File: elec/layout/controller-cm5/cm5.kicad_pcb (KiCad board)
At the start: 4 copper layers, 14 parts

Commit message: update layout, rename layout files with CM5 prefix
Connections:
- CN1 pad 12: cm5-line-7 -> cm5-line-3
- CN1 pad 15: line-1 -> line-2
- CN1 pad 17: line-2 -> line-6
- CN1 pad 19: cm5-line-4 -> cm5-line-2
- CN1 pad 20: line-6 -> line-1
- CN1 pad 23: cm5-line-5 -> cm5-line-1
- CN1 pad 25: cm5-line-2 -> cm5-line-4
- CN1 pad 27: line-7 -> line-3
- CN1 pad 40: line-3 -> line-7
- CN1 pad 41: line-4 -> line-5
- CN1 pad 78: cm5-line-3 -> cm5-line-7
- CN1 pad 80: cm5-line-1 -> cm5-line-5
- CN1 pad 81: line -> line-4
- CN1 pad 82: line-5 -> line
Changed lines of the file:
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@@
 	(net 0 "")
 	(net 1 "pins[20]")
-	(net 2 "cm5-line-3")
+	(net 2 "cm5-line-7")
 	(net 3 "cm5-pins[62]")
 	(net 4 "cm5.hdi_a-pins[74]")
@@
 	(net 7 "cm5.hdi_b-pins[74]")
 	(net 8 "cm5.hdi_a-pins[62]")
-	(net 9 "line-7")
+	(net 9 "line-3")
 	(net 10 "pins[18]")
 	(net 11 "cm5-pins[46]")
@@
 	(net 22 "cm5.hdi_a-pins[68]")
 	(net 23 "cm5.hdi_a-pins[92]")
-	(net 24 "line-4")
+	(net 24 "line-5")
 	(net 25 "pins[8]")
 	(net 26 "pins[1]")
@@
 	(net 28 "pins[90]")
 	(net 29 "pins[82]")
-	(net 30 "line-1")
+	(net 30 "line-2")
 	(net 31 "pins[58]")
 	(net 32 "SDA")
@@
 	(net 36 "cm5.hdi_a-pins[88]")
 	(net 37 "HDMI1_D2_P")
-	(net 38 "line-5")
+	(net 38 "line")
 	(net 39 "HDMI1_CK_N")
-	(net 40 "line-3")
+	(net 40 "line-7")
 	(net 41 "pins[86]")
 	(net 42 "cm5-pins[99]")
@@
 	(net 49 "cm5.hdi_b-pins[88]")
 	(net 50 "cm5.hdi_b-pins[92]")
-	(net 51 "cm5-line-4")
-	(net 52 "cm5-line-7")
+	(net 51 "cm5-line-2")
+	(net 52 "cm5-line-3")
 	(net 53 "pins[29]")
 	(net 54 "pins[49]")
@@
 	(net 71 "rj45.connector-net-1")
 	(net 72 "N_C_")
-	(net 73 "cm5-line-5")
+	(net 73 "cm5-line-1")
 	(net 74 "pins[3]")
 	(net 75 "HDMI0_CK_P")
@@
 	(net 80 "pins[41]")
 	(net 81 "pins[70]")
-	(net 82 "cm5-line-2")
+	(net 82 "cm5-line-4")
 	(net 83 "cm5.hdi_a-pins[98]")
 	(net 84 "cm5.hdi_b-pins[34]")
@@
 	(net 90 "pins[40]")
 	(net 91 "pins[91]")
-	(net 92 "line-6")
+	(net 92 "line-1")
 	(net 93 "pins[64]")
 	(net 94 "pins[9]")
@@
 	(net 116 "HDMI0_D2_P")
 	(net 117 "pins[22]")
-	(net 118 "line-2")
+	(net 118 "line-6")
 	(net 119 "pins[80]")
 	(net 120 "cm5.hdi_b-pins[94]")
@@
 	(net 125 "cm5.hdi_a-pins[94]")
 	(net 126 "cm5.hdi_a-pins[34]")
-	(net 127 "cm5-line-1")
+	(net 127 "cm5-line-5")
 	(net 128 "pins[61]")
 	(net 129 "cm5-pins[56]")
@@
 	(net 133 "pins[32]")
 	(net 134 "cm5.hdi_b-pins[93]")
-	(net 135 "line")
+	(net 135 "line-4")
 	(net 136 "cm5-pins[98]")
 	(net 137 "ETH_P0_P")
@@
 			(size 0.2 0.7)
 			(layers "F.Cu" "F.Paste" "F.Mask")
-			(net 52 "cm5-line-7")
+			(net 52 "cm5-line-3")
 		)
 		(pad "13" smd rect
@@
 			(size 0.2 0.7)
 			(layers "F.Cu" "F.Paste" "F.Mask")
-			(net 30 "line-1")
+			(net 30 "line-2")
 		)
 		(pad "16" smd rect
@@
 			(size 0.2 0.7)
 			(layers "F.Cu" "F.Paste" "F.Mask")
-			(net 118 "line-2")
+			(net 118 "line-6")
 		)
 		(pad "18" smd rect
@@
 			(size 0.2 0.7)
 			(layers "F.Cu" "F.Paste" "F.Mask")
-			(net 51 "cm5-line-4")
+			(net 51 "cm5-line-2")
 		)
 		(pad "20" smd rect
@@
 			(size 0.2 0.7)
 			(layers "F.Cu" "F.Paste" "F.Mask")
-			(net 92 "line-6")
+			(net 92 "line-1")
 		)
 		(pad "21" smd rect
@@
 			(size 0.2 0.7)
 			(layers "F.Cu" "F.Paste" "F.Mask")
-			(net 73 "cm5-line-5")
+			(net 73 "cm5-line-1")
 		)
 		(pad "24" smd rect
@@
 			(size 0.2 0.7)
 			(layers "F.Cu" "F.Paste" "F.Mask")
-			(net 82 "cm5-line-2")
+			(net 82 "cm5-line-4")
 		)
 		(pad "26" smd rect
@@
 			(size 0.2 0.7)
 			(layers "F.Cu" "F.Paste" "F.Mask")
-			(net 9 "line-7")
+			(net 9 "line-3")
 		)
 		(pad "28" smd rect
@@
 			(size 0.2 0.7)
 			(layers "F.Cu" "F.Paste" "F.Mask")
-			(net 40 "line-3")
+			(net 40 "line-7")
 		)
 		(pad "41" smd rect
@@
 			(size 0.2 0.7)
 			(layers "F.Cu" "F.Paste" "F.Mask")
-			(net 24 "line-4")
+			(net 24 "line-5")
 		)
 		(pad "42" smd rect
@@
 			(size 0.2 0.7)
 			(layers "F.Cu" "F.Paste" "F.Mask")
-			(net 2 "cm5-line-3")
+			(net 2 "cm5-line-7")
 		)
 		(pad "79" smd rect
@@
 			(size 0.2 0.7)
 			(layers "F.Cu" "F.Paste" "F.Mask")
-			(net 127 "cm5-line-1")
+			(net 127 "cm5-line-5")
 		)
 		(pad "81" smd rect
@@
 			(size 0.2 0.7)
 			(layers "F.Cu" "F.Paste" "F.Mask")
-			(net 135 "line")
+			(net 135 "line-4")
 		)
 		(pad "82" smd rect
@@
 			(size 0.2 0.7)
 			(layers "F.Cu" "F.Paste" "F.Mask")
-			(net 38 "line-5")
+			(net 38 "line")
 		)
 		(pad "83" smd rect

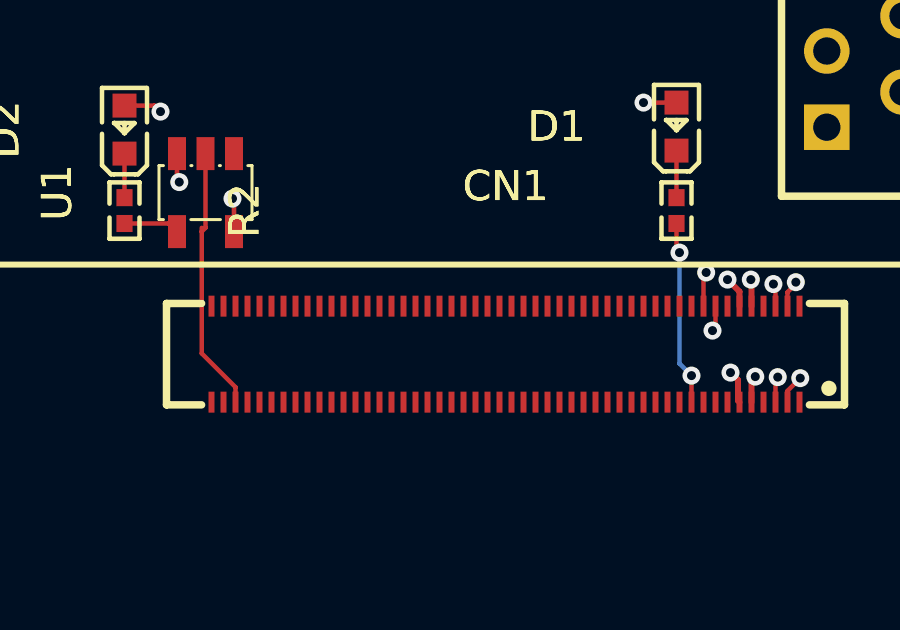
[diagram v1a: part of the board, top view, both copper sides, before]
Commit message: update layouts to kicad 9
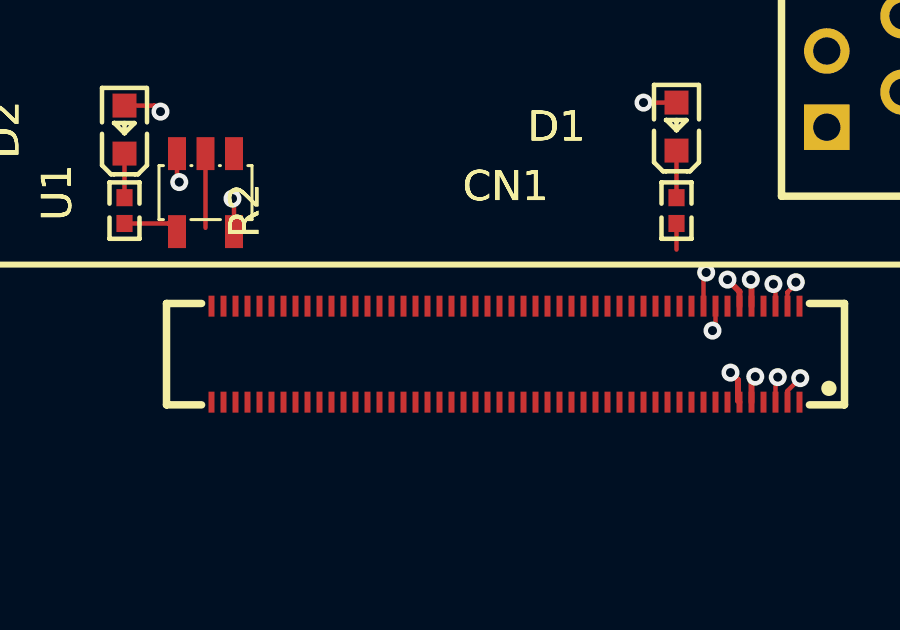
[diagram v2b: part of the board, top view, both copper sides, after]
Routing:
- net PWR_LED: track 8.93 -> 2.47 mm
- net pins[19]: track 6.16 -> 0.87 mm, vias 2 -> 0

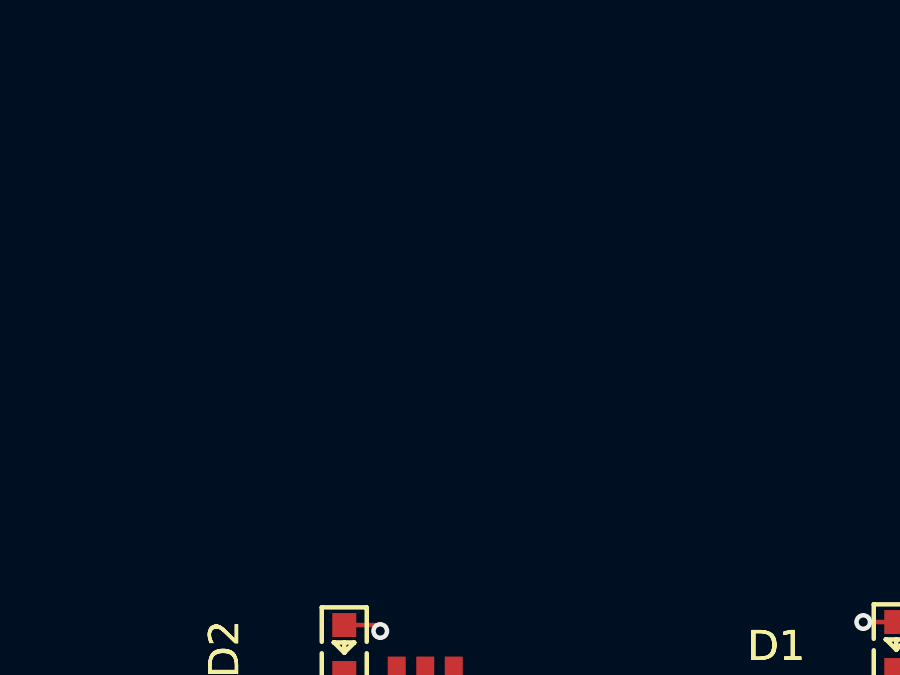
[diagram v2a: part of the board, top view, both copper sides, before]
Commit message: add power button and boot button, fix CAN layout
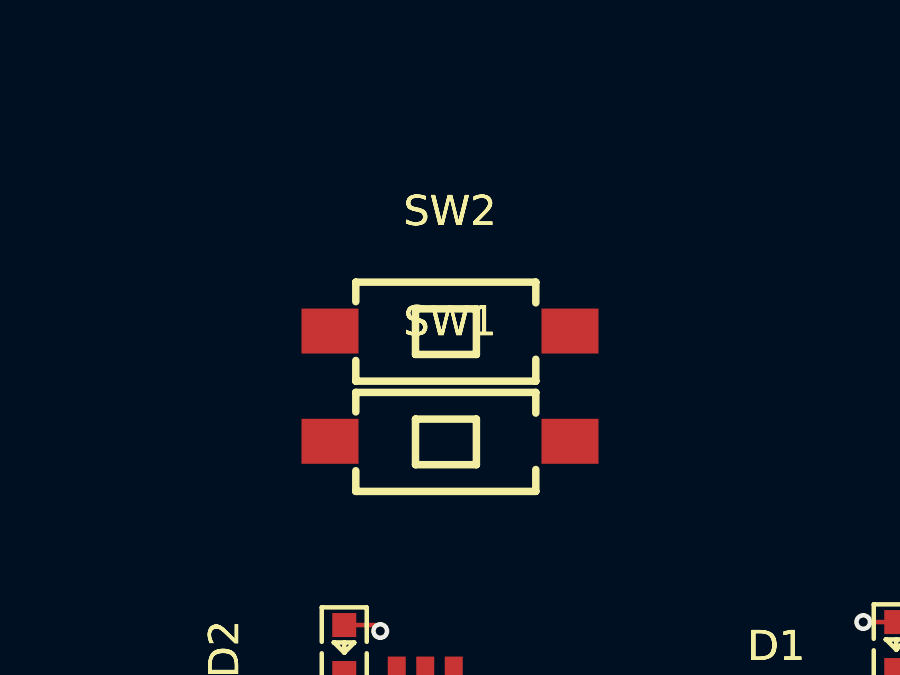
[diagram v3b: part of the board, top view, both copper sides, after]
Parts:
- added SW1: , atopile:SW-SMD_L6.0-W3.3-LS8.0-cfbaed, F.Cu at (140.7, 88.9)
- added SW2: , atopile:SW-SMD_L6.0-W3.3-LS8.0-cfbaed, F.Cu at (140.7, 85.2)
- R1, R2: value 10kΩ ±1% 62.5mW -> 2kΩ ±1% 62.5mW
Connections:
- net ETH_LED_ACTIVITY renamed line-31
- net ETH_LED_LINK renamed line-20
- net ETH_P0_N renamed line-41
- net ETH_P1_N renamed line-10
- net ETH_P1_P renamed line-28
- net ETH_P2_N renamed line-14
- net ETH_P3_N renamed line-37
- net ETH_P3_P renamed line-8
- net HDMI0_CK_N renamed pins[89]
- net HDMI0_CK_P renamed cm5-pins[87]
- net HDMI0_D0_N renamed pins[83]
- net HDMI0_D0_P renamed cm5-pins[81]
- net HDMI0_D1_N renamed pins[77]
- net HDMI0_D1_P renamed cm5-pins[75]
- net HDMI0_D2_N renamed cm5-pins[71]
- net HDMI0_D2_P renamed cm5-pins[69]
- net HDMI0_HOTPLUG renamed pins[52]
- net HDMI1_CEC renamed pins[48]
- net HDMI1_CK_N renamed pins[65]
- net HDMI1_CK_P renamed cm5-pins[63]
- net HDMI1_D0_N renamed pins[59]
- net HDMI1_D0_P renamed pins[57]
- net HDMI1_D1_N renamed pins[53]
- net HDMI1_D1_P renamed pins[51]
- net HDMI1_D2_P renamed pins[45]
- net HDMI1_HOTPLUG renamed pins[42]
- net SCL renamed line-9
- net SDA renamed line-34
- net UART_RX renamed line-26
- net UART_TX renamed line-12
- net USB2_D_N renamed line-38
- net VCC_1V8 renamed cm5-pins[87]-1
- net VCC_3V3 renamed hv
- net VCC_5V renamed pins[78]
- net cm5-line-6 renamed line-11
- net cm5-line-7 renamed cm5-pins[44]
- net cm5-pins[26] renamed line-30
- net cm5-pins[46] renamed pins[46]
- net cm5-pins[46]-1 renamed line-36
- net cm5-pins[68] renamed line-23
- net cm5.hdi_a-pins[34] renamed line-25
- net cm5.hdi_a-pins[56] renamed pins[56]
- net cm5.hdi_a-pins[62] renamed pins[62]
- net cm5.hdi_a-pins[68] renamed pins[68]
- net cm5.hdi_b-pins[26] renamed pins[26]
- net cm5.hdi_b-pins[34] renamed pins[34]
- net cm5.hdi_b-pins[92] renamed pins[92]
- net pins[20] renamed cm5.hdi_b-pins[20]
- net pins[23] renamed cm5.hdi_b-pins[23]
- net pins[29] renamed line-24
- net pins[39] renamed line-39
- net pins[41] renamed line-29
- net pins[43] renamed line-42
- net pins[44] renamed cm5-pins[44]-1
- net pins[58] renamed line-27
- net pins[63] renamed cm5.hdi_a-pins[63]
- net pins[64] renamed line-43
- net pins[69] renamed cm5.hdi_a-pins[69]
- net pins[70] renamed line-15
- net pins[71] renamed cm5.hdi_a-pins[71]
- net pins[75] renamed cm5.hdi_a-pins[75]
- net pins[95] renamed cm5.hdi_b-pins[95]
- CN1 pad 12: cm5-line-3 -> cm5-pins[23]
- CN1 pad 13: I2S_WS -> cm5-line-5
- CN1 pad 15: line-2 -> line-16
- CN1 pad 17: line-6 -> pins[33]
- CN1 pad 18: cm5.hdi_a-pins[35] -> line-7
- CN1 pad 19: cm5-line-2 -> line-17
- CN1 pad 20: line-1 -> line-21
- CN1 pad 23: cm5-line-1 -> line-6
- CN1 pad 24: pins[47] -> cm5-line-3
- CN1 pad 25: cm5-line-4 -> line-32
- CN1 pad 27: line-3 -> cm5-line-2
- CN1 pad 40: line-7 -> pins[79]
- CN1 pad 41: line-5 -> cm5.hdi_a-pins[81]
- CN1 pad 46: pins[91] -> line-33
- CN1 pad 48: PWR_LED -> cm5.hdi_a-pins[95]
- CN1 pad 53: cm5.hdi_a-pins[94] -> cm5-pins[94]
- CN1 pad 54: cm5.hdi_a-pins[92] -> line-13
- CN1 pad 6: ETH_P0_P -> line-4
- CN1 pad 75: pins[50] -> line-35
- CN1 pad 76: I2S_SCK -> cm5-line
- CN1 pad 80: cm5-line-5 -> cm5-line-1
- CN1 pad 81: line-4 -> line-22
- CN1 pad 82: line -> line-19
- CN1 pad 85: cm5-line -> line-18
- CN1 pad 88: I2S_SD -> cm5-line-4
- CN1 pad 90: gnd -> cm5-pins[20]
- CN1 pad 95: ETH_P2_P -> line
- CN2 pad 17: pins[33] -> line-40
- CN2 pad 18: cm5-pins[35] -> line-2
- CN2 pad 24: HDMI1_D2_N -> pins[47]
- CN2 pad 69: cm5-pins[62] -> line-1
- CN2 pad 72: cm5-pins[56] -> line-3
- CN2 pad 75: HDMI0_CEC -> pins[50]
- CN2 pad 98: USB2_D_P -> line-5
- R1 pad 2: pins[19] -> cm5-pins[20]
- RJ1 pad P2: ETH_P0_P -> line-4
- RJ1 pad P5: ETH_P2_P -> line
- U1 pad 2: PWR_LED -> cm5-pins[94]
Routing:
- net line-4: track 0.00 -> 16.5 mm, vias 0 -> 1
- net ETH_P0_P: track 16.5 -> 0.00 mm, vias 1 -> 0
- net line: track 0.00 -> 13.3 mm, vias 0 -> 1
- net ETH_P2_P: track 13.3 -> 0.00 mm, vias 1 -> 0
- net cm5-pins[94]: track 0.00 -> 2.47 mm
- net PWR_LED: track 2.47 -> 0.00 mm
- net pins[19]: track 0.87 -> 0.00 mm
- net cm5-pins[20]: track 0.00 -> 0.87 mm

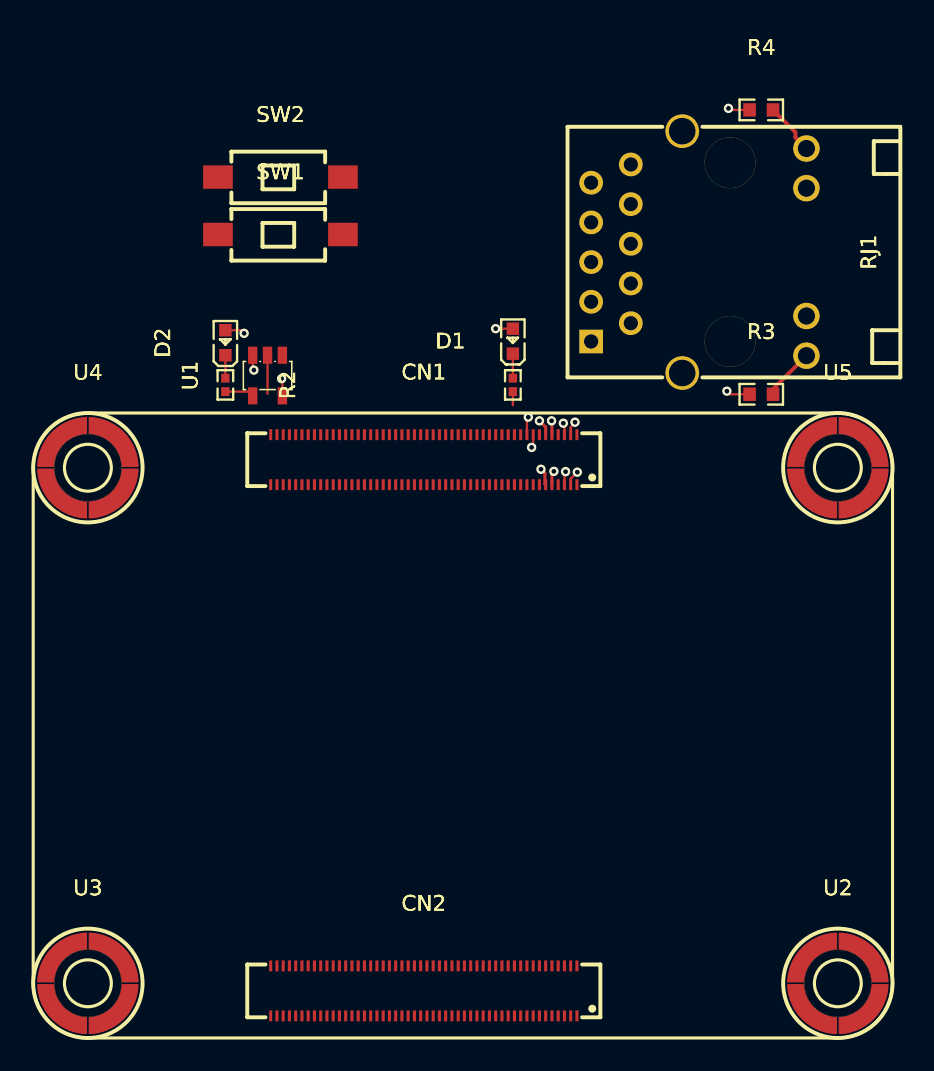
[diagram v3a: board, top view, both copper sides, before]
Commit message: update cm5 controller layout
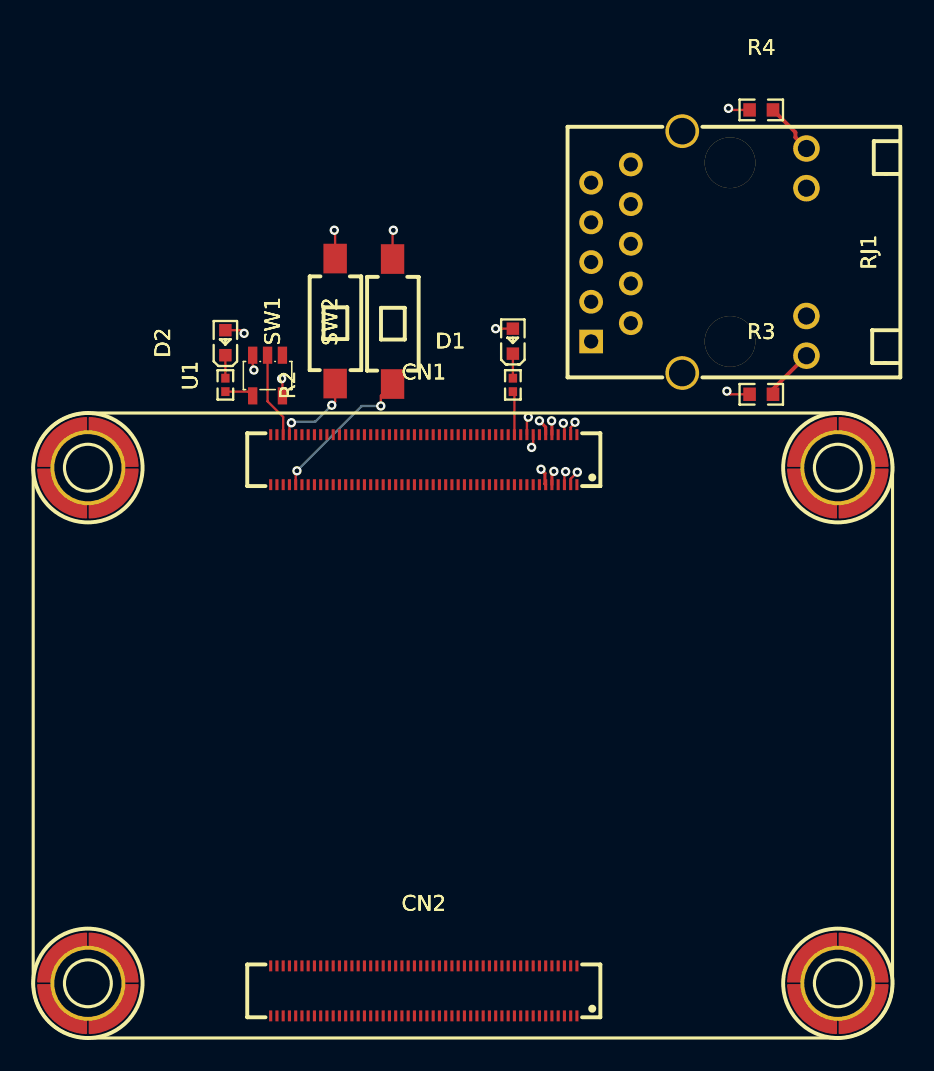
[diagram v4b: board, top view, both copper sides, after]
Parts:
- U2, U3, U4, U5: footprint atopile:SMD_BD5.6-D4.1-12eb58 -> lib:SMD_BD5.6-D4.1-12eb58
- moved SW2 11.7 mm to (147.9, 94.4), turned to 90 degrees
- moved SW1 6.55 mm to (144.2, 94.4), turned to 90 degrees
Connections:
- net cm5-line renamed cm5-pins[48]-1
- net cm5-line-1 renamed cm5-pins[40]
- net cm5-line-2 renamed cm5-pins[53]
- net cm5-line-3 renamed cm5-pins[47]
- net cm5-line-4 renamed pins[24]
- net cm5-line-5 renamed pins[25]
- net line-14 renamed MDI2_
- net line-15 renamed pins[70]
- net line-17 renamed pins[37]
- net line-18 renamed pins[30]
- net line-2 renamed pins[35]
- net line-21 renamed pins[39]-1
- net line-24 renamed pins[29]
- net line-26 renamed pins[54]
- net line-27 renamed pins[58]
- net line-28 renamed MDI1plus
- net line-29 renamed pins[41]
- net line-33 renamed pins[91]
- net line-37 renamed pins[4]-1
- net line-38 renamed pins[2]
- net line-39 renamed pins[39]
- net line-4 renamed MDI0plus
- net line-41 renamed MDI0_
- net line-42 renamed pins[43]
- net line-43 renamed pins[64]
- net line-5 renamed pins[4]
- net line-7 renamed pins[35]-1
- net line-8 renamed MDI3plus
- net line-9 renamed pins[55]
- net pins[40] renamed cm5.hdi_b-pins[40]
- net pins[47] renamed cm5-pins[47]-1
- net pins[48] renamed cm5-pins[48]
- net pins[53] renamed cm5-pins[53]-1
- CN1 pad 14: line-12 -> pins[27]
- CN1 pad 15: line-16 -> line
- CN1 pad 17: pins[33] -> cm5-pins[33]
- CN1 pad 23: line-6 -> pins[45]
- CN1 pad 25: line-32 -> pins[49]
- CN1 pad 29: line-34 -> pins[57]
- CN1 pad 3: line-10 -> pins[5]
- CN1 pad 54: line-13 -> pins[92]
- CN1 pad 66: pins[68] -> cm5.hdi_a-pins[68]
- CN1 pad 69: pins[62] -> cm5.hdi_a-pins[62]
- CN1 pad 72: pins[56] -> cm5.hdi_a-pins[56]
- CN1 pad 75: line-35 -> pins[50]
- CN1 pad 77: line-36 -> pins[46]
- CN1 pad 78: cm5-pins[44] -> cm5-pins[44]-1
- CN1 pad 81: line-22 -> pins[38]
- CN1 pad 82: line-19 -> line-1
- CN1 pad 83: line-25 -> pins[34]
- CN1 pad 86: line-11 -> pins[28]
- CN1 pad 87: line-30 -> pins[26]
- CN1 pad 92: line-31 -> pins[16]
- CN1 pad 93: line-20 -> pins[14]
- CN1 pad 95: line -> pins[10]
- CN2 pad 14: pins[27] -> cm5.hdi_b-pins[27]
- CN2 pad 17: line-40 -> pins[33]
- CN2 pad 23: pins[45] -> cm5-pins[45]
- CN2 pad 25: pins[49] -> cm5.hdi_b-pins[49]
- CN2 pad 29: pins[57] -> cm5-pins[57]
- CN2 pad 3: pins[5] -> cm5.hdi_b-pins[5]
- CN2 pad 54: pins[92] -> cm5.hdi_b-pins[92]
- CN2 pad 66: line-23 -> pins[68]
- CN2 pad 69: line-1 -> pins[62]
- CN2 pad 72: line-3 -> pins[56]
- CN2 pad 75: pins[50] -> cm5-pins[50]
- CN2 pad 77: pins[46] -> cm5-pins[46]
- CN2 pad 78: cm5-pins[44]-1 -> cm5-pins[44]
- CN2 pad 81: pins[38] -> cm5.hdi_b-pins[38]
- CN2 pad 83: pins[34] -> cm5.hdi_b-pins[34]
- CN2 pad 86: pins[28] -> cm5.hdi_b-pins[28]
- CN2 pad 87: pins[26] -> cm5.hdi_b-pins[26]
- CN2 pad 92: pins[16] -> cm5.hdi_b-pins[16]
- CN2 pad 93: pins[14] -> cm5.hdi_b-pins[14]
- CN2 pad 95: pins[10] -> cm5.hdi_b-pins[10]
- D1 pad 1: cm5-cathode -> cm5-cathode-1
- D2 pad 1: cm5-cathode-1 -> cm5-cathode
- R1 pad 1: cm5-cathode -> cm5-cathode-1
- R2 pad 1: cm5-cathode-1 -> cm5-cathode
- RJ1 pad 12: line-20 -> pins[14]
- RJ1 pad 13: line-31 -> pins[16]
- RJ1 pad P1: rj45.connector-net -> rj45.connector-net-1
- RJ1 pad P10: rj45.connector-net-1 -> rj45.connector-net
- RJ1 pad P5: line -> pins[10]
- RJ1 pad P7: line-10 -> pins[5]
- SW1 pad 1: line-13 -> pins[92]
- U2 pad 1: stud1-net -> gnd
- U3 pad 1: stud2-net -> gnd
- U4 pad 1: stud3-net -> gnd
- U5 pad 1: stud4-net -> gnd
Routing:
- net pins[16]: track 0.00 -> 29.5 mm, vias 0 -> 1
- net line-31: track 29.5 -> 0.00 mm, vias 1 -> 0
- net pins[14]: track 0.00 -> 24.6 mm, vias 0 -> 1
- net line-20: track 24.6 -> 0.00 mm, vias 1 -> 0
- net pins[5]: track 0.00 -> 18.8 mm, vias 0 -> 1
- net line-10: track 18.8 -> 0.00 mm, vias 1 -> 0
- net pins[10]: track 0.00 -> 13.3 mm, vias 0 -> 1
- net line: track 13.3 -> 0.00 mm, vias 1 -> 0
- net pins[91]: track 0.00 -> 9.73 mm, vias 0 -> 2
- net pins[92]: track 0.00 -> 5.35 mm, vias 0 -> 2
- net gnd: track 0.98 -> 4.68 mm, vias 1 -> 3
- net cm5-pins[94]: track 2.47 -> 5.50 mm
- net cm5-pins[20]: track 0.87 -> 2.80 mm
